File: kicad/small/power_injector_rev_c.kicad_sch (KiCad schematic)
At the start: 15 parts, among them J2 A00-108-220-450, J3 A00-108-220-450, J4 JACK-PLUG0

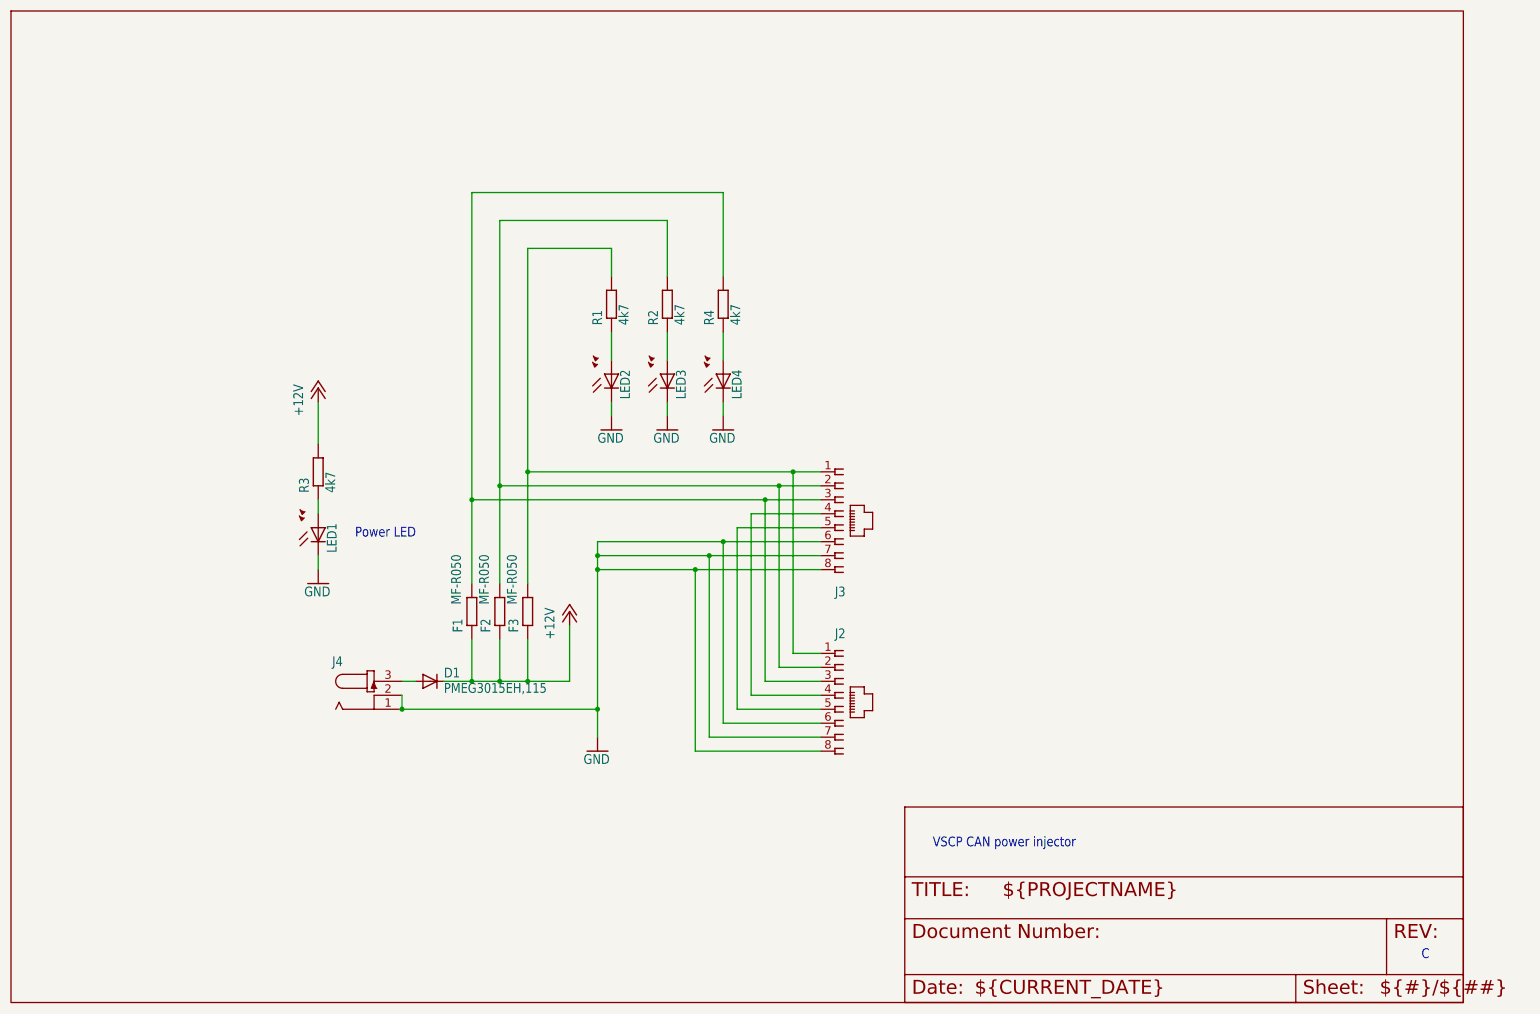
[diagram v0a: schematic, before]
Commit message: Rearranged files (in a more logical way)
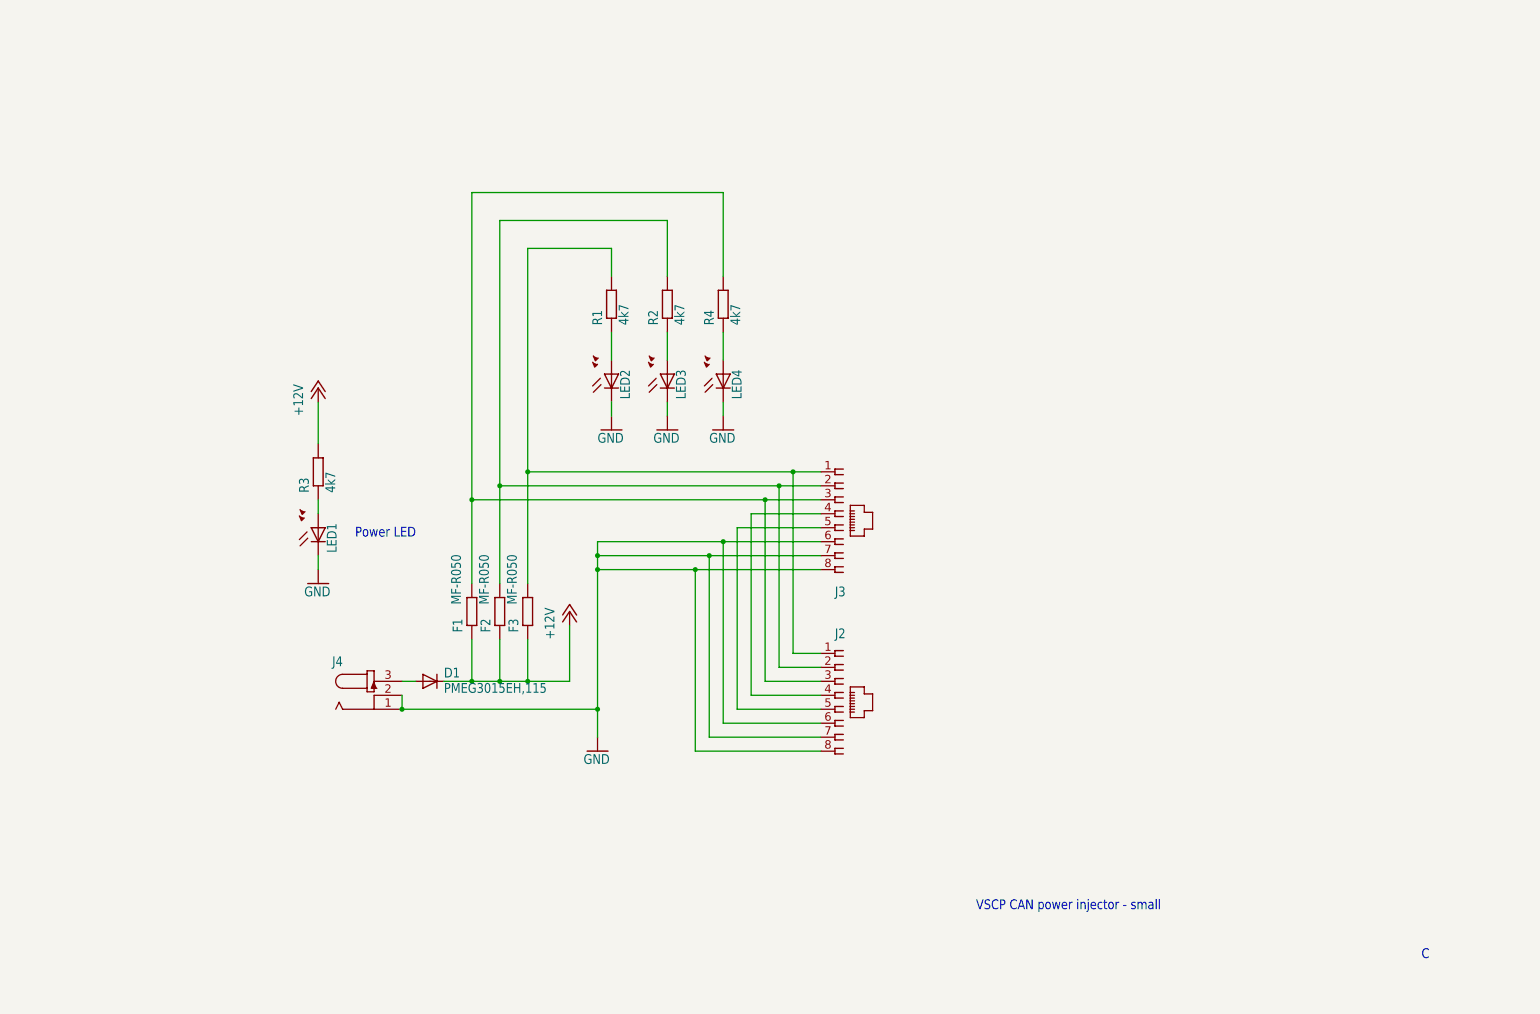
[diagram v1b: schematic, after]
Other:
- note added: "VSCP CAN power injector - small"
- note removed: "VSCP CAN power injector"
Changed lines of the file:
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@@
 		)
 	)
-	(text "VSCP CAN power injector"
+	(text "VSCP CAN power injector - small"
 		(exclude_from_sim no)
-		(at 185.42 170.18 0)
+		(at 193.294 181.61 0)
 		(effects
 			(font
@@
 	)
 	(symbol
-		(lib_id "power_injector_rev_c-eagle-import:DINA4_L")
-		(at 180.34 198.12 0)
-		(unit 2)
-		(exclude_from_sim no)
-		(in_bom yes)
-		(on_board yes)
-		(dnp no)
-		(property "Reference" "#FRAME1"
-			(at 180.34 198.12 0)
-			(effects
-				(font
-					(size 1.27 1.27)
-				)
-				(hide yes)
-			)
-		)
-		(property "Value" "DINA4_L"
-			(at 180.34 198.12 0)
-			(effects
-				(font
-					(size 1.27 1.27)
-				)
-				(hide yes)
-			)
-		)
-		(property "Footprint" ""
-			(at 180.34 198.12 0)
-			(effects
-				(font
-					(size 1.27 1.27)
-				)
-				(hide yes)
-			)
-		)
-		(property "Datasheet" ""
-			(at 180.34 198.12 0)
-			(effects
-				(font
-					(size 1.27 1.27)
-				)
-				(hide yes)
-			)
-		)
-		(property "Description" ""
-			(at 180.34 198.12 0)
-			(effects
-				(font
-					(size 1.27 1.27)
-				)
-				(hide yes)
-			)
-		)
-		(instances
-			(project ""
-				(path "/47bd3032-e417-4aa5-813e-5d6dc8479352"
-					(reference "#FRAME1")
-					(unit 2)
-				)
-			)
-		)
-	)
-	(symbol
 		(lib_id "power_injector_rev_c-eagle-import:GND")
 		(at 137.16 93.98 0)
@@
 					(unit 1)
 				)
-			)
-		)
-	)
-	(symbol
-		(lib_id "power_injector_rev_c-eagle-import:DINA4_L")
-		(at 17.78 198.12 0)
-		(unit 1)
-		(exclude_from_sim no)
-		(in_bom yes)
-		(on_board yes)
-		(dnp no)
-		(property "Reference" "#FRAME1"
-			(at 17.78 198.12 0)
-			(effects
-				(font
-					(size 1.27 1.27)
-				)
-				(hide yes)
-			)
-		)
-		(property "Value" "DINA4_L"
-			(at 17.78 198.12 0)
-			(effects
-				(font
-					(size 1.27 1.27)
-				)
-				(hide yes)
-			)
-		)
-		(property "Footprint" ""
-			(at 17.78 198.12 0)
-			(effects
-				(font
-					(size 1.27 1.27)
-				)
-				(hide yes)
-			)
-		)
-		(property "Datasheet" ""
-			(at 17.78 198.12 0)
-			(effects
-				(font
-					(size 1.27 1.27)
-				)
-				(hide yes)
-			)
-		)
-		(property "Description" ""
-			(at 17.78 198.12 0)
-			(effects
-				(font
-					(size 1.27 1.27)
-				)
-				(hide yes)
-			)
-		)
-		(instances
-			(project ""
-				(path "/47bd3032-e417-4aa5-813e-5d6dc8479352"
-					(reference "#FRAME1")
-					(unit 1)
-				)
